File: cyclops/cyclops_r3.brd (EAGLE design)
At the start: 124.5 x 79.9 mm, 144 parts, among them Q1 BC817, Q2 IRF510, Q3 BC817, T0 0, T1 0, T2 0, T3 0, U1 MCP4921, U10 TLV2374, U11 THS4281, U12 MAX4564, U13 ZXTD, U14 ZXTD, U2 ADG3301, U3 MAX4564, U4 LT1931, U5 LT1764A, U6 337L, U7 TLV3701, U8 ADR03, U9 OP1177, X1 SLP3, X2 SLP3, X3 SLP3

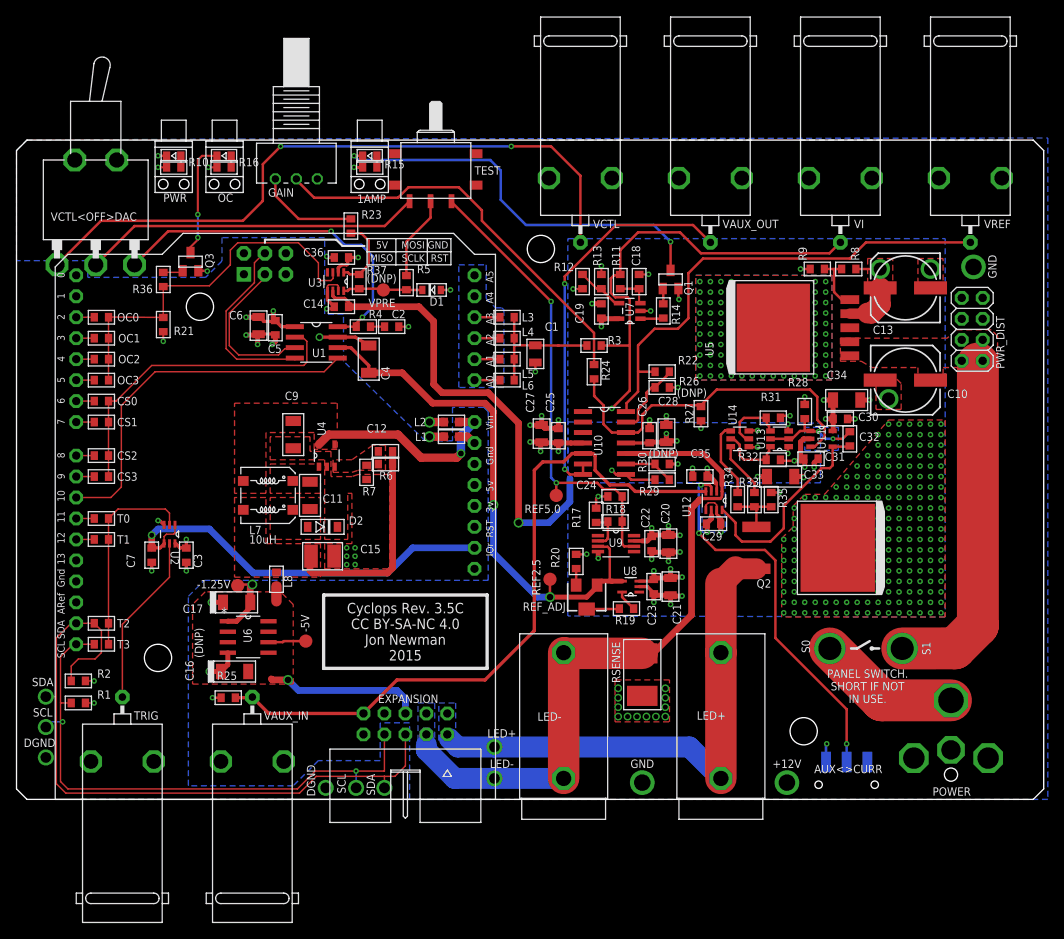
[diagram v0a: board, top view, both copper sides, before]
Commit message: First round of proofing revisions after building rev 3.5c board.
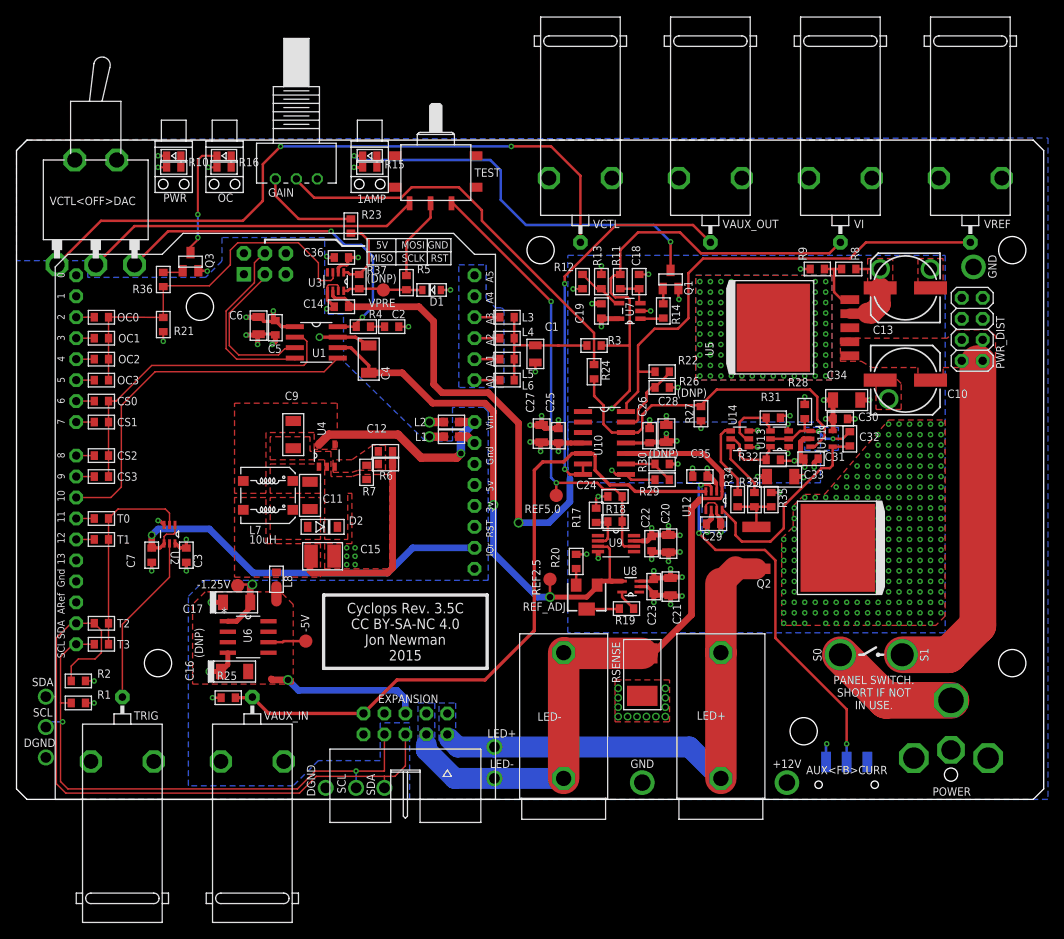
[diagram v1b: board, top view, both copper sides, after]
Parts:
- moved HEATSINK 2.03 mm to (112.5, 20.2)
- moved TEST 0.25 mm to (50.8, 76.1)
- renumbered AUX<>CURR to AUX<FB>CURR
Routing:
- net POW_IN: track 17.3 -> 15.7 mm
- net N$14: track 10.5 -> 11.0 mm
- net +12V: vias 208 -> 222
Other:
- board text added: "DAC<OFF>VCTL"

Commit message: Refactored library for rev. 3.5c.
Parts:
- R21: value 10k -> 220k
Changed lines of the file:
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@@
 <?xml version="1.0" encoding="utf-8"?>
 <!DOCTYPE eagle SYSTEM "eagle.dtd">
-<eagle version="6.5.0">
+<eagle version="7.5.0">
 <drawing>
 <settings>
@@
 <pass name="Default">
 <param name="RoutingGrid" value="25mil"/>
+<param name="AutoGrid" value="1"/>
+<param name="Efforts" value="0"/>
+<param name="TopRouterVariant" value="1"/>
 <param name="tpViaShape" value="round"/>
 <param name="PrefDir.1" value="|"/>
@@
 <attribute name="VALUE" x="37.35" y="62.033" size="1.016" layer="27" font="vector" ratio="18" rot="R180"/>
 </element>
-<element name="R21" library="cyclops" package="0603" value="10k" x="17.78" y="57.531" smashed="yes" rot="R270">
+<element name="R21" library="cyclops" package="0603" value="220k" x="17.78" y="57.531" smashed="yes" rot="R270">
 <attribute name="MN" value="Panasonic" x="17.78" y="57.531" size="1.016" layer="27" font="vector" rot="R270" display="off"/>
 <attribute name="DK" value="PxxxxHTR-ND" x="17.78" y="57.531" size="1.016" layer="27" font="vector" rot="R270" display="off"/>

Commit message: Final changes to board after rev 3.5c construction and testing.
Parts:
- R21: value 220k -> 110k
- R36: value 10k -> 2.2k
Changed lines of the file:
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@@
 <?xml version="1.0" encoding="utf-8"?>
 <!DOCTYPE eagle SYSTEM "eagle.dtd">
-<eagle version="7.5.0">
+<eagle version="6.5.0">
 <drawing>
 <settings>
@@
 <text x="62.992" y="13.97" size="2.1844" layer="22" font="vector" ratio="18" rot="MR180" align="center">Cyclops
 Rev. 3.5C</text>
-<text x="109.982" y="17.526" size="1.016" layer="21" font="vector" ratio="18" rot="R270" align="center">S1</text>
-<text x="97.028" y="17.526" size="1.016" layer="21" font="vector" ratio="18" rot="R90" align="center">S0</text>
-<wire x1="102.108" y1="17.526" x2="102.616" y2="17.526" width="0.3048" layer="21"/>
+<text x="109.728" y="17.526" size="1.016" layer="21" font="vector" ratio="18" rot="R270" align="center">S1</text>
+<text x="97.282" y="17.526" size="1.016" layer="21" font="vector" ratio="18" rot="R90" align="center">S0</text>
+<wire x1="101.854" y1="17.526" x2="102.616" y2="17.526" width="0.3048" layer="21"/>
 <wire x1="102.616" y1="17.526" x2="104.14" y2="18.415" width="0.3048" layer="21"/>
 <circle x="104.394" y="17.526" radius="0.127" width="0.3048" layer="21"/>
-<wire x1="104.521" y1="17.526" x2="105.029" y2="17.526" width="0.3048" layer="21"/>
+<wire x1="104.521" y1="17.526" x2="105.283" y2="17.526" width="0.3048" layer="21"/>
 <text x="103.886" y="12.954" size="1.016" layer="21" font="vector" ratio="18" align="center">PANEL SWITCH.
 SHORT IF NOT
@@
 <pass name="Default">
 <param name="RoutingGrid" value="25mil"/>
-<param name="AutoGrid" value="1"/>
-<param name="Efforts" value="0"/>
-<param name="TopRouterVariant" value="1"/>
 <param name="tpViaShape" value="round"/>
 <param name="PrefDir.1" value="|"/>
@@
 <attribute name="VALUE" x="37.35" y="62.033" size="1.016" layer="27" font="vector" ratio="18" rot="R180"/>
 </element>
-<element name="R21" library="cyclops" package="0603" value="220k" x="17.78" y="57.531" smashed="yes" rot="R270">
+<element name="R21" library="cyclops" package="0603" value="110k" x="17.78" y="57.531" smashed="yes" rot="R270">
 <attribute name="MN" value="Panasonic" x="17.78" y="57.531" size="1.016" layer="27" font="vector" rot="R270" display="off"/>
 <attribute name="DK" value="PxxxxHTR-ND" x="17.78" y="57.531" size="1.016" layer="27" font="vector" rot="R270" display="off"/>
@@
 <attribute name="VALUE" x="25.146" y="63.119" size="1.016" layer="27" font="vector" ratio="18" rot="R90"/>
 </element>
-<element name="R36" library="cyclops" package="0603" value="10k" x="17.78" y="62.992" smashed="yes" rot="R270">
+<element name="R36" library="cyclops" package="0603" value="2.2k" x="17.78" y="62.992" smashed="yes" rot="R270">
 <attribute name="MN" value="Panasonic" x="17.78" y="62.992" size="1.016" layer="27" font="vector" rot="R270" display="off"/>
 <attribute name="DK" value="PxxxxHTR-ND" x="17.78" y="62.992" size="1.016" layer="27" font="vector" rot="R270" display="off"/>
@@
 <contactref element="PWR_DIST" pad="2"/>
 <contactref element="PWR_DIST" pad="4"/>
-<via x="107.315" y="17.526" extent="1-16" drill="2.8" diameter="0.3302" shape="octagon"/>
+<via x="107.315" y="17.526" extent="1-16" drill="2.2" diameter="0.3302" shape="octagon"/>
 <wire x1="116.348" y1="53.864" x2="116.348" y2="53.862" width="0.3048" layer="1"/>
 <contactref element="U5" pad="2"/>
@@
 <signal name="POW_IN" class="1">
 <contactref element="POWER" pad="1"/>
-<via x="99.822" y="17.526" extent="1-16" drill="2.8" diameter="0.3302" shape="octagon"/>
+<via x="99.822" y="17.526" extent="1-16" drill="2.2" diameter="0.3302" shape="octagon"/>
 <wire x1="113.224" y1="12" x2="105.348" y2="12" width="4.445" layer="1"/>
 <wire x1="99.822" y1="17.526" x2="105.348" y2="12" width="4.445" layer="1"/>
